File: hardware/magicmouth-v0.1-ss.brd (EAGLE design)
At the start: 100 x 80 mm, 35 parts, among them IC1 LM386N, IC2 ATMEGA168-20P, Q1 16Mhz, U1 ARDUINOR3-NOIOREF-NOTEXT

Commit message: connected reset button to GND not +5V
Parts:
- removed R7: 4K7, rcl:0207/7
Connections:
- removed net N$34: R7.2, S1.3
- net +5V: no longer R7.1
- net GND: now also S1.3
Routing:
- net N$34: track 14.2 -> 0.00 mm
- net GND: track 155.7 -> 165.0 mm
- net +5V: track 71.4 -> 69.8 mm
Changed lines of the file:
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@@
 <setting verticaltext="up"/>
 </settings>
-<grid distance="0.025" unitdist="inch" unit="inch" style="lines" multiple="1" display="yes" altdistance="0.025" altunitdist="inch" altunit="inch"/>
+<grid distance="0.025" unitdist="inch" unit="mm" style="lines" multiple="1" display="yes" altdistance="0.025" altunitdist="inch" altunit="inch"/>
 <layers>
 <layer number="1" name="Top" color="4" fill="1" visible="yes" active="yes"/>
@@
 <attribute name="NAME" x="43.434" y="26.035" size="1.27" layer="25" ratio="10"/>
 </element>
-<element name="R7" library="rcl" package="0207/7" value="4K7" x="44.45" y="33.655" smashed="yes" rot="R180">
-<attribute name="RESISTANCE" value="4K7" x="44.45" y="33.655" size="1.778" layer="27" rot="R180" display="off"/>
-<attribute name="NAME" x="45.593" y="34.29" size="1.27" layer="25" ratio="10" rot="R180"/>
-</element>
 <element name="JP9" library="SparkFun-Connectors" package="1X01NS" value="M01SMDNS" x="51.816" y="55.88"/>
 <element name="R8" library="rcl" package="0207/7" value="220K" x="22.225" y="58.42" smashed="yes" rot="R90">
@@
 <wire x1="35.56" y1="33.655" x2="36.83" y2="33.655" width="0.4064" layer="16"/>
 <wire x1="36.83" y1="33.655" x2="39.37" y2="31.115" width="0.4064" layer="16"/>
-<wire x1="39.37" y1="31.115" x2="39.37" y2="21.082" width="0.4064" layer="16"/>
+<wire x1="39.37" y1="31.115" x2="39.37" y2="26.67" width="0.4064" layer="16"/>
+<wire x1="39.37" y1="26.67" x2="39.37" y2="21.082" width="0.4064" layer="16"/>
 <wire x1="35.56" y1="33.655" x2="35.433" y2="33.655" width="0.4064" layer="16"/>
 <wire x1="35.433" y1="33.655" x2="35.306" y2="33.782" width="0.4064" layer="16"/>
@@
 <wire x1="31.496" y1="52.07" x2="31.496" y2="55.753" width="0.4064" layer="16"/>
 <wire x1="31.496" y1="55.753" x2="31.369" y2="55.88" width="0.4064" layer="16"/>
+<contactref element="S1" pad="3"/>
+<wire x1="46.7106" y1="23.4188" x2="46.7106" y2="24.4094" width="0.4064" layer="16"/>
+<wire x1="46.7106" y1="24.4094" x2="44.45" y2="26.67" width="0.4064" layer="16"/>
+<wire x1="44.45" y1="26.67" x2="39.37" y2="26.67" width="0.4064" layer="16"/>
 </signal>
 <signal name="N$2">
@@
 <via x="54.61" y="16.51" extent="1-16" drill="0.8" diameter="1.6764"/>
 <wire x1="62.865" y1="38.735" x2="65.096525" y2="40.948471875" width="0.4064" layer="16"/>
-<contactref element="R7" pad="1"/>
 <wire x1="40.64" y1="16.51" x2="45.72" y2="16.51" width="0.4064" layer="16"/>
 <wire x1="45.72" y1="16.51" x2="48.26" y2="13.97" width="0.4064" layer="16"/>
 <wire x1="48.26" y1="19.685" x2="48.26" y2="19.05" width="0.4064" layer="16"/>
 <wire x1="48.26" y1="19.05" x2="45.72" y2="16.51" width="0.4064" layer="16"/>
-<wire x1="48.26" y1="33.655" x2="49.375921875" y2="32.539078125" width="0.4064" layer="16"/>
 <wire x1="49.375921875" y1="32.539078125" x2="49.375921875" y2="20.800921875" width="0.4064" layer="16"/>
 <wire x1="49.375921875" y1="20.800921875" x2="48.26" y2="19.685" width="0.4064" layer="16"/>
@@
 <wire x1="46.736" y1="58.42" x2="46.736" y2="60.96" width="0.4064" layer="16"/>
 </signal>
-<signal name="N$34">
-<contactref element="R7" pad="2"/>
-<contactref element="S1" pad="3"/>
-<wire x1="46.7106" y1="23.4188" x2="46.7106" y2="24.4094" width="0.4064" layer="16"/>
-<wire x1="46.7106" y1="24.4094" x2="44.45" y2="26.67" width="0.4064" layer="16"/>
-<wire x1="44.45" y1="26.67" x2="44.45" y2="32.385" width="0.4064" layer="16"/>
-<wire x1="44.45" y1="32.385" x2="43.18" y2="33.655" width="0.4064" layer="16"/>
-<wire x1="43.18" y1="33.655" x2="40.64" y2="33.655" width="0.4064" layer="16"/>
-</signal>
 <signal name="N$35">

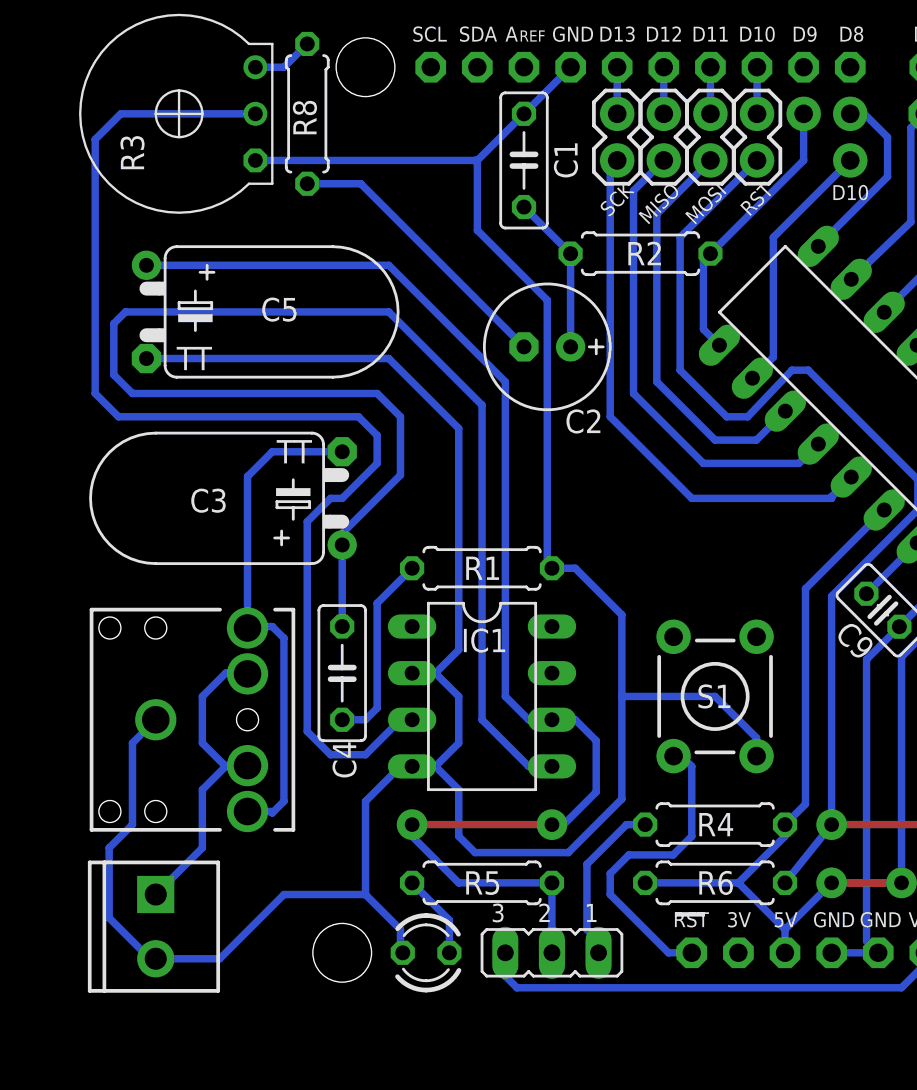
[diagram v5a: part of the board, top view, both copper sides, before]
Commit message: adjusted placement to avoid through holes directly above Arduino USB port
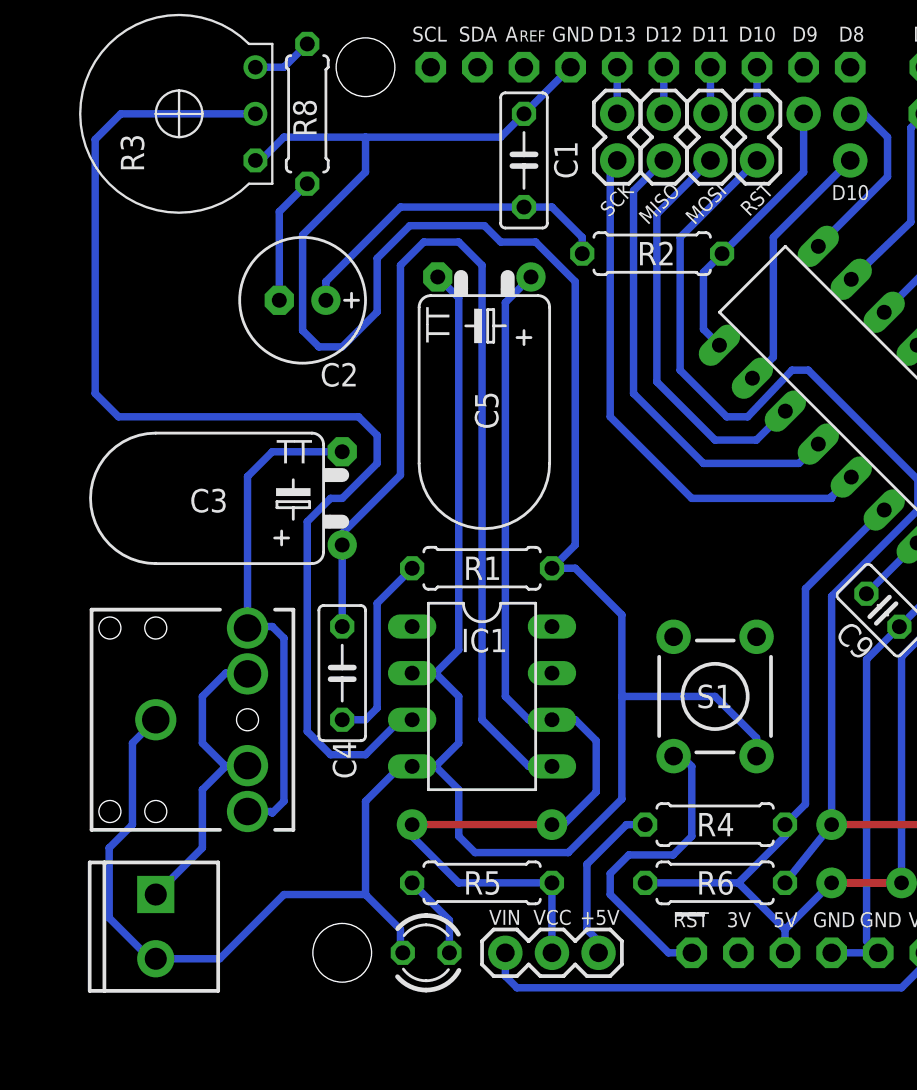
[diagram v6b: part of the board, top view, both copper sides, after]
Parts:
- JP1: value (none) -> JUMPER-3PTH; device jumper:JP2 -> SparkFun-Passives:1X03
- moved C5 18.5 mm to (31.9, 49.5), turned to 180 degrees
- moved C2 13.6 mm to (22.0, 48.3)
- moved JP1 2.54 mm to (38.1, 12.7)
- moved R2 0.63 mm to (41.0, 50.8)
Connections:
- removed net VS: C5.+, IC1.6, JP1.2, R5.2
- new net VIN: JP1.3, U1.VIN
- net VCC: now also C5.+, IC1.6, JP1.2, R5.2; no longer JP1.3, U1.VIN
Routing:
- net VS: track 72.0 -> 0.00 mm, vias 2 -> 0
- net VCC: track 25.6 -> 56.1 mm, vias 0 -> 2
- net VIN: track 0.00 -> 25.6 mm
- net N$1: track 76.5 -> 56.1 mm
- net GND: track 165.0 -> 179.9 mm
- net N$2: track 8.67 -> 18.2 mm
- net N$5: track 15.5 -> 6.98 mm
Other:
- board text added: "+5V"
- board text added: "VCC"

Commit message: adjusted placement to avoid through holes directly above Arduino USB port
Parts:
- IC2: value ATMEGA168-20P -> ATMEGA328P_PDIP; device adafruit:DIL28-3 -> SparkFun-DigitalIC:DIL28-3
- moved U$1 2.54 mm to (55.2, 25.4)
- moved IC2 0.90 mm to (58.4, 36.2)
- moved R3 0.63 mm to (14.6, 58.4)
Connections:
- net MOSI: no longer IC2.17
- net N$11: no longer IC2.10
- net N$12: no longer IC2.16
- net N$13: no longer IC2.23
- net N$16: no longer IC2.2
- net N$31: no longer IC2.28
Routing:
- net GND1: track 49.0 -> 51.9 mm
- net MOSI: track 22.2 -> 20.0 mm
- net N$13: track 18.1 -> 16.3 mm
- net N$12: track 14.1 -> 12.5 mm
- net SIGNAL: track 15.2 -> 14.0 mm
- net N$23: track 10.7 -> 11.7 mm
- net N$21: track 14.9 -> 15.8 mm
- net N$22: track 12.8 -> 13.7 mm
- net MISO: track 25.5 -> 24.6 mm
- net SCK: track 29.6 -> 28.7 mm
- net N$20: track 25.5 -> 26.4 mm
- net N$34: track 3.91 -> 3.01 mm
- net +5V: track 69.8 -> 68.9 mm
- net N$30: track 14.3 -> 13.4 mm
- net N$15: track 16.5 -> 15.6 mm
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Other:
- board text added: "http://is.gd/magicmouth"
- board text removed: "http://tinyurl.com/magicmouth"
